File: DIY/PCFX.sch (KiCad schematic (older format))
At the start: 5 parts, among them J1 PCFX, J2 PCFX, J3 DB25_Male, U1 74AHCT125N, U2 74AHCT125N

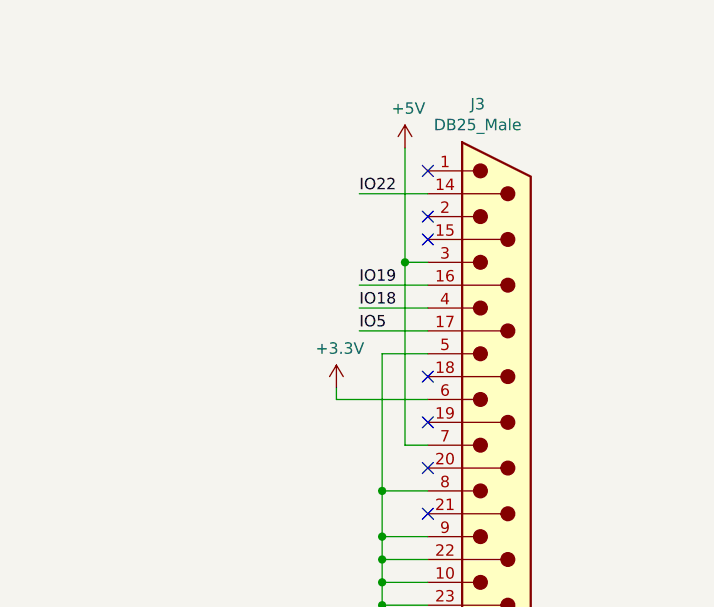
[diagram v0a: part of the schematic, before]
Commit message: [DIY] Fixup PC-FX DB25 pin3 and add CD-i cable adapter
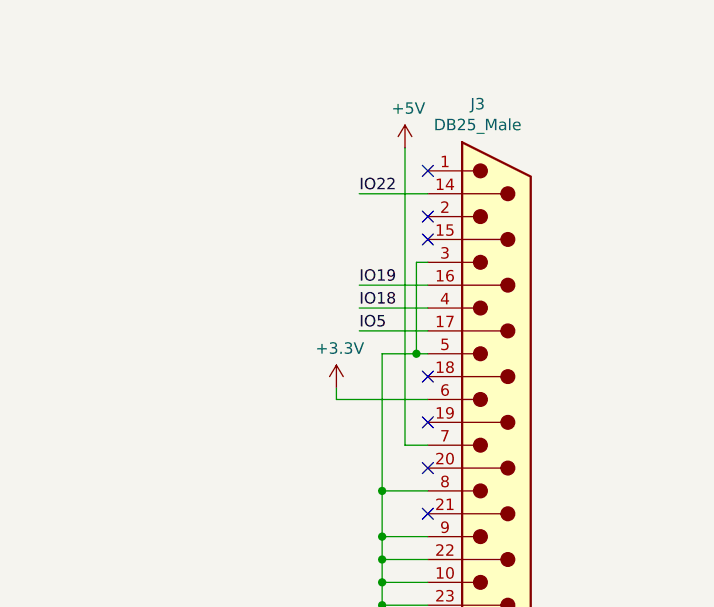
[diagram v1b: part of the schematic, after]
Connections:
- net +5V: no longer J3.3
- net GND: now also J3.3
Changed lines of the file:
@@
 $Descr A4 11693 8268
 encoding utf-8
-Sheet 13 13
+Sheet 13 14
 Title "BlueRetro - PC-FX adapter cable"
-Date "2021-04-01"
-Rev "v1.0"
+Date "2021-04-11"
+Rev "v1.1"
 Comp "©2021 Jacques Gagnon, licensed under CC-BY-4.0"
 Comment1 ""
@@
 $EndComp
 Wire Wire Line
-	10250 2150 10050 2150
+	10250 2150 10200 2150
 Wire Wire Line
 	10250 2950 10050 2950
-Wire Wire Line
-	10150 1250 10150 1750
 Wire Wire Line
 	10150 2550 10250 2550
@@
 IO33
 Wire Wire Line
-	10250 1750 10150 1750
-Connection ~ 10150 1750
-Wire Wire Line
-	10150 1750 10150 2550
-Wire Wire Line
 	10250 3350 10050 3350
 Connection ~ 10050 3350
@@
 Text Label 2000 3800 2    50   ~ 0
 P2-CLK
+Wire Wire Line
+	10150 1250 10150 2550
+Wire Wire Line
+	10250 1750 10200 1750
+Wire Wire Line
+	10200 1750 10200 2150
+Connection ~ 10200 2150
+Wire Wire Line
+	10200 2150 10050 2150
 $EndSCHEMATC
